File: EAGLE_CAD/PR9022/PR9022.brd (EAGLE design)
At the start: 70 x 70 mm, 73 parts

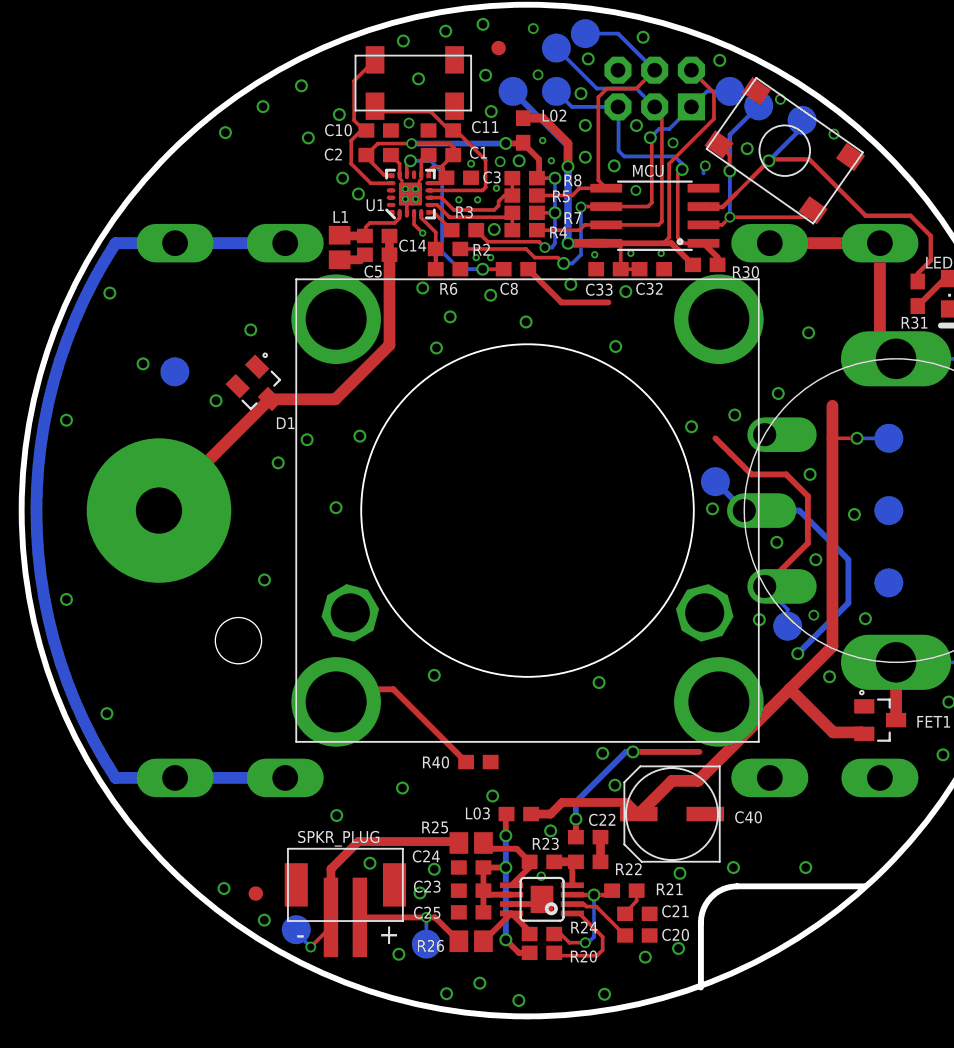
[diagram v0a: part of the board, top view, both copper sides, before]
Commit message: Updated PR9022 Layout
Rotated AMP circuitry 90deg
Added spacing on C23, C24, C25, C21, R21
Added updated speaker footprint w/M3 PemNuts
Added updated antenna footprint w/M3 PemNuts
Rerouted MCU traced to accommodate new SPK placement
Rerouted power, and audio traces to accommodate new SPK placement
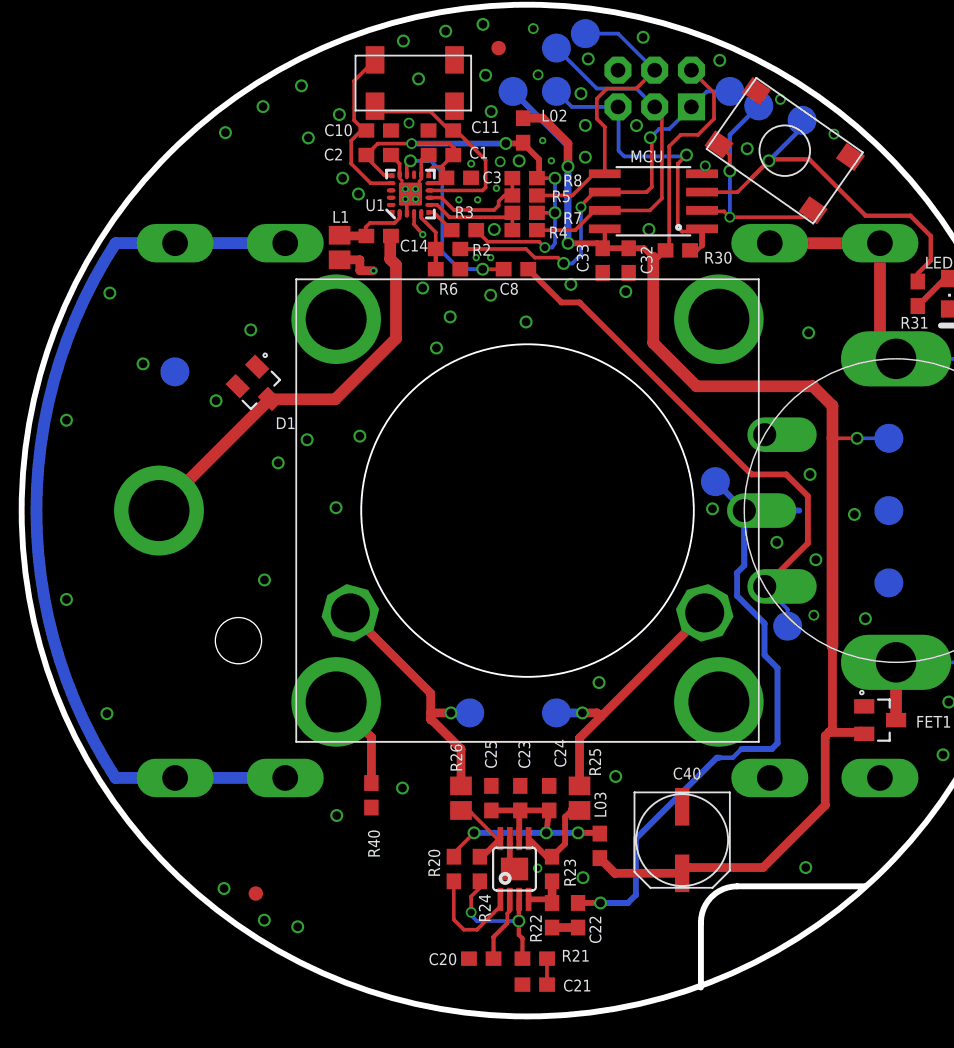
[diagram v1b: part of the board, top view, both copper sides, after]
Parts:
- removed C5: DNP, PR_Parts_Library:0603_CPL
- removed SPKR_PLUG: (no value), PR_Parts_Library:JST-B2B-PH-SM4-TB
- ANT_MOUNT: device PR_Parts_Library:M3_BOLT_HOLE -> PR_Parts_Library:PEM_M3
- moved T6 23.4 mm to (37.0, 21.0)
- moved T7 16.3 mm to (31.0, 21.0)
- moved C20 10.9 mm to (31.8, 4.00), turned to 0 degrees
- moved R26 9.92 mm to (30.4, 15.1), turned to 90 degrees
- moved C21 8.63 mm to (35.5, 2.20), turned to 0 degrees
- moved R20 8.42 mm to (29.9, 10.2), turned to 90 degrees
- moved R25 8.12 mm to (38.6, 15.1), turned to 90 degrees
- moved C25 8.02 mm to (32.5, 15.1), turned to 90 degrees
- moved R21 7.78 mm to (35.5, 4.00)
- moved R40 7.75 mm to (24.2, 15.3), turned to 90 degrees
- moved C23 7.25 mm to (34.5, 15.1), turned to 90 degrees
- moved C24 7.22 mm to (36.5, 15.1), turned to 90 degrees
- moved R24 6.22 mm to (31.7, 10.2), turned to 270 degrees
- moved L03 6.02 mm to (40.0, 11.8), turned to 90 degrees
- moved C22 5.45 mm to (38.5, 7.00), turned to 90 degrees
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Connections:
- net ANT: now also ANT_MOUNT.P$2; no longer ANT_MOUNT.P$1, C5.1
- net GND: no longer C5.2
- net SPK_OUT+: now also SPKR_PLACE.P$6; no longer SPKR_PLUG.2
- net SPK_OUT-: now also SPKR_PLACE.P$5; no longer SPKR_PLUG.1
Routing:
- net VCC: track 100.2 -> 114.4 mm
- net A_OUT: track 32.0 -> 44.8 mm, vias 3 -> 1
- net A_IN: track 25.5 -> 36.8 mm
- net SPK_OUT-: track 9.38 -> 17.9 mm
- net N$8: track 10.2 -> 6.62 mm
- net SPK_OUT+: track 17.2 -> 18.7 mm
- net N$5: track 8.95 -> 10.3 mm
- net SCLK: track 25.6 -> 24.6 mm
- net N$2: track 17.6 -> 18.5 mm
- net N$11: track 4.69 -> 5.50 mm
- net GND: track 16.1 -> 16.8 mm, vias 111 -> 87
- net SDIO: track 22.1 -> 21.4 mm
- net !RST: track 28.8 -> 28.2 mm
- net LED/PB4: track 26.8 -> 26.2 mm
- net N$4: track 6.02 -> 6.57 mm

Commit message: Small Changes
Updated the library to incorporate single M3_Pemnuts
Used these parts to build out the speaker connection points
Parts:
- added U$2, U$3, U$4: PEM_M3_NOPIN, PR_Parts_Library:PEM_M3_NOKEEPAWAY
- added U$5: PEM_M3_W/PIN, PR_Parts_Library:PEM_M3_NOKEEPAWAY
- moved L1 1.28 mm to (23.0, 54.0)
- moved T7 1.00 mm to (32.0, 21.0)
- moved C14 0.10 mm to (24.7, 53.9), turned to 90 degrees
- turned R40 to 270 degrees
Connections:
- removed net N$8: R40.2, SPKR_PLACE.P$4
- new net N$6: R40.1, U$5.P$2
- net GND: now also R40.2; no longer R40.1
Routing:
- net N$8: track 6.62 -> 0.00 mm
- net N$6: track 0.00 -> 6.62 mm
- net N$16: track 5.43 -> 3.89 mm
- net ANT: track 28.7 -> 29.9 mm
- net SPK_OUT-: track 17.9 -> 18.9 mm
- net GND: track 16.8 -> 17.5 mm, vias 87 -> 91
